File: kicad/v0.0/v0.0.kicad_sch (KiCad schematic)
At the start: 18 parts, among them M1 MNMOS, M2 MNMOS, U1 OPAMP, U2 MAX14872ETC+, U3 NE555D

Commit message: kicad stuff
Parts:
- added C?: 1uF, Capacitor_SMD:C_0805_2012Metric_Pad1.18x1.45mm_HandSolder, symbol Device:C_Small
- added J?: BUTTON, Connector_Molex:Molex_KK-254_AE-6410-02A_1x02_P2.54mm_Vertical, symbol Connector_Generic:Conn_01x02
- added R?: 10k, Resistor_SMD:R_0805_2012Metric_Pad1.20x1.40mm_HandSolder, symbol Device:R
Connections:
- net GND: now also C?.2, J?.1 (Pin_1)
- net at U2.6 (REV): now also M2.4 (B); no longer M2.1 (D)
- net at M1.1 (D), U3.3 (Q): now also M2.1 (D); no longer M2.3 (S), M2.4 (B)
- new net: J?.2 (Pin_2), R?.1
- new net BUTTON: C?.1, R?.2
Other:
- note added: "BUTTON"
- note added: "LED"
- note added: "MOTOR CONTROLLER"
- note added: "POWER/STEP-DOWN"
- note added: "PROCESSOR CONNECTORS"
- note removed: "MOTOR IC"
- note removed: "must choose R that keeps |V_COM| < 250mV"
- note removed: "use FAULT to tell microP that theres a problem? or just ground FAULT and CPU ignores if theres an error?"
- moved on the sheet: C1, C2, C3, D1, D2, D3, D4, M1, M2, R3, R4, R5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

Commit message: v0.0 is done (i think)! also added a Documents folder to store datasheets and such
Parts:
- added J?: ESP8266_left, symbol Connector:Conn_01x15_Female
- added J?: USB_B_Micro, symbol Connector:USB_B_Micro
- added J?: LED, symbol Connector:Conn_01x02_Male
- added J?: ESP8266_right, symbol Connector:Conn_01x15_Female
- added R? (x2): 10k, symbol Device:R
- added R?: R, symbol Device:R
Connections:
- net +5V: now also J?.1 (VBUS)
- net BUTTON: now also J?.2 (Pin_2)
- net FWD: now also J?.3 (Pin_3)
- net GND: now also J?.1 (Pin_1), J?.10 (Pin_10), J?.14 (Pin_14), J?.14 (Pin_14), J?.5 (GND), J?.7 (Pin_7), R?.2, R?.2, R?.2
- net REV: now also J?.4 (Pin_4)
- net V_PHOTO: now also J?.1 (Pin_1)
- new net: J?.2 (D-), R?.1
- new net: J?.3 (D+), R?.1
- new net: J?.6 (Shield), R?.1
- new net: J?.13 (Pin_13), J?.2 (Pin_2)
- new net 3V3: J?.11 (Pin_11), J?.15 (Pin_15), J?.6 (Pin_6)
- new net A0: J?.1 (Pin_1)
- new net CLK: J?.9 (Pin_9)
- new net CMD: J?.7 (Pin_7)
- new net D4: J?.5 (Pin_5)
- new net D5: J?.8 (Pin_8)
- new net D6: J?.9 (Pin_9)
- new net D7: J?.10 (Pin_10)
- new net D8: J?.11 (Pin_11)
- new net D9: J?.12 (Pin_12)
- new net EN: J?.12 (Pin_12)
- new net RST: J?.13 (Pin_13)
- new net RSV: J?.2 (Pin_2), J?.3 (Pin_3)
- new net SD0: J?.8 (Pin_8)
- new net SD1: J?.6 (Pin_6)
- new net SD2: J?.5 (Pin_5)
- new net SD3: J?.4 (Pin_4)
- new net Vin: J?.15 (Pin_15)
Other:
- note added: "POWER"
- note removed: "LED"
- note removed: "POWER/STEP-DOWN"
- moved on the sheet: C?, J?, R?

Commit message: forgot to save in kicad before sending files here... awk
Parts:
- removed J?: USB_B_Micro, symbol Connector:USB_B_Micro
- removed R? (x2): 10k, symbol Device:R
- removed R?: R, symbol Device:R
- added C5: 470u, symbol pspice:C
- added C6: 220u, symbol pspice:C
- added D5: D_Schottky, symbol Device:D_Schottky
- added J2: 9V_IN, symbol Connector:Barrel_Jack
- added L1: 68u, symbol pspice:INDUCTOR
- added U4: LM2596S-5, Package_TO_SOT_SMD:TO-263-5_TabPin3, symbol Regulator_Switching:LM2596S-5
- gave numbers to parts that had none: 6
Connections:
- net +5V: now also C6.1, L1.2, U4.4 (FB)
- net GND: now also C5.1, C6.2, D5.2 (A), J2.2, U4.3 (GND), U4.5 (~{ON}/OFF)
- new net: D5.1 (K), L1.1, U4.2 (OUT)
- new net +9V: C5.2, J2.1, U4.1 (VIN)
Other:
- note added: "POWER INPUT"
- note removed: "POWER"

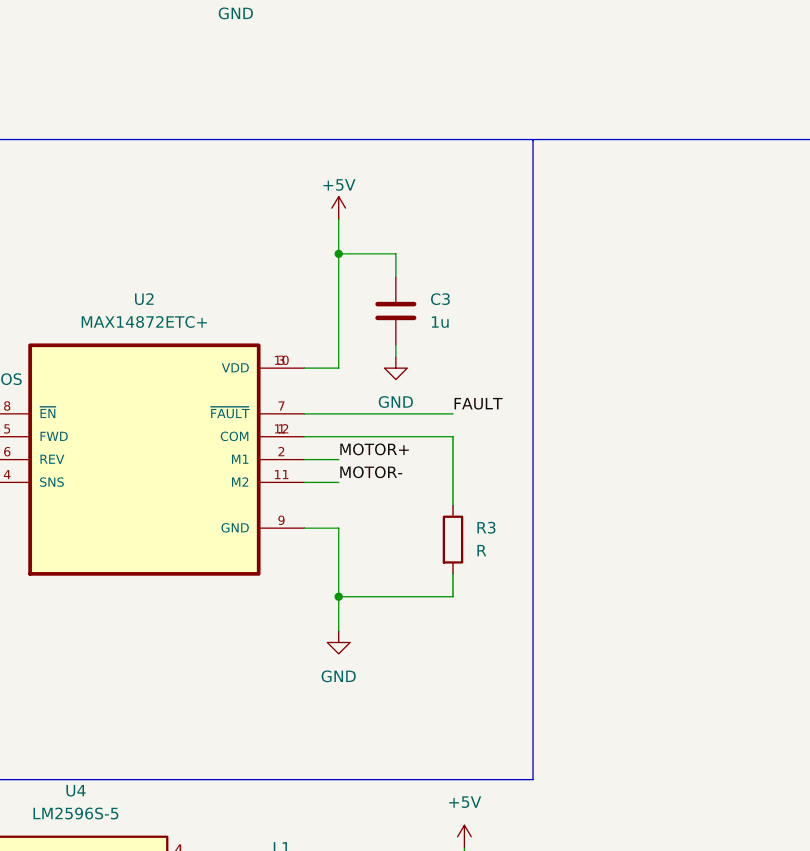
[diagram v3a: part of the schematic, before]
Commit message: updated motor to be 9V
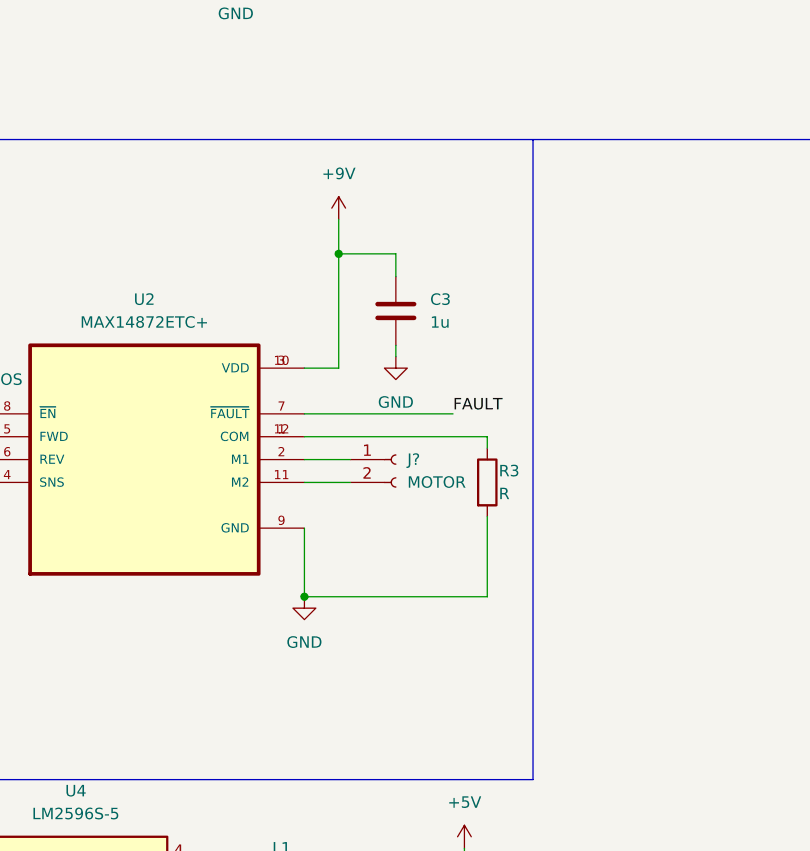
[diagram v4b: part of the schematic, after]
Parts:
- added J?: MOTOR, symbol Connector:Conn_01x02_Female
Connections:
- net +5V: no longer C3.1, U2.10 (VDD), U2.3 (VDD)
- net +9V: now also C3.1, U2.10 (VDD), U2.3 (VDD)
- net MOTOR+: no longer names the net of U2.2 (M1)
- net MOTOR+: now also J?.1 (Pin_1)
- net MOTOR-: no longer names the net of U2.11 (M2)
- net MOTOR-: now also J?.2 (Pin_2)
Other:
- moved on the sheet: R3
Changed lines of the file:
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@@
   (junction (at 39.37 181.61) (diameter 0) (color 0 0 0 0)
   )
+  (junction (at 153.67 144.78) (diameter 0) (color 0 0 0 0)
+  )
   (junction (at 100.33 193.04) (diameter 0) (color 0 0 0 0)
   )
-  (junction (at 157.48 144.78) (diameter 0) (color 0 0 0 0)
-  )
   (junction (at 45.72 114.3) (diameter 0) (color 0 0 0 0)
   )
@@
     (stroke (width 0) (type default) (color 0 0 0 0))
   )
+  (wire (pts (xy 173.99 128.27) (xy 173.99 127))
+    (stroke (width 0) (type default) (color 0 0 0 0))
+  )
   (wire (pts (xy 15.24 105.41) (xy 21.59 105.41))
     (stroke (width 0) (type default) (color 0 0 0 0))
@@
     (stroke (width 0) (type default) (color 0 0 0 0))
   )
+  (wire (pts (xy 153.67 137.16) (xy 153.67 144.78))
+    (stroke (width 0) (type default) (color 0 0 0 0))
+  )
   (wire (pts (xy 100.33 179.07) (xy 100.33 193.04))
     (stroke (width 0) (type default) (color 0 0 0 0))
@@
     (stroke (width 0) (type default) (color 0 0 0 0))
   )
+  (wire (pts (xy 153.67 132.08) (xy 158.75 132.08))
+    (stroke (width 0) (type default) (color 0 0 0 0))
+  )
   (wire (pts (xy 73.66 43.18) (xy 77.47 43.18))
     (stroke (width 0) (type default) (color 0 0 0 0))
@@
     (stroke (width 0) (type default) (color 0 0 0 0))
   )
+  (wire (pts (xy 153.67 144.78) (xy 173.99 144.78))
+    (stroke (width 0) (type default) (color 0 0 0 0))
+  )
   (wire (pts (xy 110.49 187.96) (xy 110.49 193.04))
     (stroke (width 0) (type default) (color 0 0 0 0))
@@
     (stroke (width 0) (type default) (color 0 0 0 0))
   )
-  (wire (pts (xy 157.48 144.78) (xy 157.48 148.59))
-    (stroke (width 0) (type default) (color 0 0 0 0))
-  )
   (wire (pts (xy 29.21 105.41) (xy 33.02 105.41))
     (stroke (width 0) (type default) (color 0 0 0 0))
@@
     (stroke (width 0) (type default) (color 0 0 0 0))
   )
-  (wire (pts (xy 153.67 132.08) (xy 157.48 132.08))
-    (stroke (width 0) (type default) (color 0 0 0 0))
-  )
   (wire (pts (xy 52.07 121.92) (xy 52.07 114.3))
     (stroke (width 0) (type default) (color 0 0 0 0))
@@
     (stroke (width 0) (type default) (color 0 0 0 0))
   )
-  (wire (pts (xy 157.48 137.16) (xy 153.67 137.16))
-    (stroke (width 0) (type default) (color 0 0 0 0))
-  )
   (wire (pts (xy 165.1 179.07) (xy 165.1 173.99))
     (stroke (width 0) (type default) (color 0 0 0 0))
@@
     (stroke (width 0) (type default) (color 0 0 0 0))
   )
-  (wire (pts (xy 170.18 127) (xy 170.18 134.62))
-    (stroke (width 0) (type default) (color 0 0 0 0))
-  )
-  (wire (pts (xy 170.18 142.24) (xy 170.18 144.78))
-    (stroke (width 0) (type default) (color 0 0 0 0))
-  )
   (wire (pts (xy 142.24 189.23) (xy 142.24 193.04))
     (stroke (width 0) (type default) (color 0 0 0 0))
@@
     (stroke (width 0) (type default) (color 0 0 0 0))
   )
-  (wire (pts (xy 153.67 129.54) (xy 157.48 129.54))
+  (wire (pts (xy 153.67 129.54) (xy 158.75 129.54))
     (stroke (width 0) (type default) (color 0 0 0 0))
   )
@@
     (stroke (width 0) (type default) (color 0 0 0 0))
   )
-  (wire (pts (xy 153.67 127) (xy 170.18 127))
+  (wire (pts (xy 153.67 127) (xy 173.99 127))
     (stroke (width 0) (type default) (color 0 0 0 0))
   )
@@
     (stroke (width 0) (type default) (color 0 0 0 0))
   )
-  (wire (pts (xy 157.48 144.78) (xy 170.18 144.78))
-    (stroke (width 0) (type default) (color 0 0 0 0))
-  )
   (wire (pts (xy 49.53 139.7) (xy 52.07 139.7))
     (stroke (width 0) (type default) (color 0 0 0 0))
@@
     (stroke (width 0) (type default) (color 0 0 0 0))
   )
-  (wire (pts (xy 157.48 137.16) (xy 157.48 144.78))
+  (wire (pts (xy 173.99 135.89) (xy 173.99 144.78))
     (stroke (width 0) (type default) (color 0 0 0 0))
   )
@@
     (effects (font (size 1.27 1.27)) (justify left bottom))
   )
-  (label "MOTOR-" (at 157.48 132.08 0)
-    (effects (font (size 1.27 1.27)) (justify left bottom))
-  )
   (label "3V3" (at 177.8 66.04 0)
     (effects (font (size 1.27 1.27)) (justify left bottom))
@@
   )
   (label "BUTTON" (at 44.45 181.61 0)
-    (effects (font (size 1.27 1.27)) (justify left bottom))
-  )
-  (label "MOTOR+" (at 157.48 129.54 0)
     (effects (font (size 1.27 1.27)) (justify left bottom))
   )
@@
     )
     (property "Datasheet" "" (id 3) (at 163.83 118.11 0)
+      (effects (font (size 1.27 1.27)) hide)
+    )
+    (pin "1")
+  )
+  (symbol (lib_id "power:+9V") (at 157.48 102.87 0) (unit 1)
+    (in_bom yes) (on_board yes) (fields_autoplaced)
+    (property "Reference" "#PWR?" (id 0) (at 157.48 106.68 0)
+      (effects (font (size 1.27 1.27)) hide)
+    )
+    (property "Value" "+9V" (id 1) (at 157.48 97.79 0))
+    (property "Footprint" "" (id 2) (at 157.48 102.87 0)
+      (effects (font (size 1.27 1.27)) hide)
+    )
+    (property "Datasheet" "" (id 3) (at 157.48 102.87 0)
       (effects (font (size 1.27 1.27)) hide)
     )
@@
     (pin "2")
   )
+  (symbol (lib_id "Connector:Conn_01x02_Female") (at 163.83 129.54 0) (unit 1)
+    (in_bom yes) (on_board yes) (fields_autoplaced)
+    (property "Reference" "J?" (id 0) (at 165.1 129.5399 0)
+      (effects (font (size 1.27 1.27)) (justify left))
+    )
+    (property "Value" "MOTOR" (id 1) (at 165.1 132.0799 0)
+      (effects (font (size 1.27 1.27)) (justify left))
+    )
+    (property "Footprint" "" (id 2) (at 163.83 129.54 0)
+      (effects (font (size 1.27 1.27)) hide)
+    )
+    (property "Datasheet" "~" (id 3) (at 163.83 129.54 0)
+      (effects (font (size 1.27 1.27)) hide)
+    )
+    (pin "1")
+    (pin "2")
+  )
   (symbol (lib_id "Connector_Generic:Conn_01x02") (at 21.59 184.15 180) (unit 1)
     (in_bom yes) (on_board yes) (fields_autoplaced)
@@
     (pin "1")
     (pin "2")
-  )
-  (symbol (lib_id "power:+5V") (at 157.48 102.87 0) (unit 1)
-    (in_bom yes) (on_board yes)
-    (property "Reference" "#PWR06" (id 0) (at 157.48 106.68 0)
-      (effects (font (size 1.27 1.27)) hide)
-    )
-    (property "Value" "+5V" (id 1) (at 157.48 99.06 0))
-    (property "Footprint" "" (id 2) (at 157.48 102.87 0)
-      (effects (font (size 1.27 1.27)) hide)
-    )
-    (property "Datasheet" "" (id 3) (at 157.48 102.87 0)
-      (effects (font (size 1.27 1.27)) hide)
-    )
-    (pin "1")
   )
   (symbol (lib_id "Device:D") (at 52.07 125.73 270) (unit 1)
@@
     (pin "2")
   )
-  (symbol (lib_id "power:GND") (at 157.48 148.59 0) (unit 1)
-    (in_bom yes) (on_board yes) (fields_autoplaced)
-    (property "Reference" "#PWR07" (id 0) (at 157.48 154.94 0)
-      (effects (font (size 1.27 1.27)) hide)
-    )
-    (property "Value" "GND" (id 1) (at 157.48 153.67 0))
-    (property "Footprint" "" (id 2) (at 157.48 148.59 0)
-      (effects (font (size 1.27 1.27)) hide)
-    )
-    (property "Datasheet" "" (id 3) (at 157.48 148.59 0)
-      (effects (font (size 1.27 1.27)) hide)
-    )
-    (pin "1")
-  )
-  (symbol (lib_id "Device:R") (at 170.18 138.43 0) (unit 1)
+  (symbol (lib_id "power:GND") (at 153.67 144.78 0) (unit 1)
+    (in_bom yes) (on_board yes) (fields_autoplaced)
+    (property "Reference" "#PWR07" (id 0) (at 153.67 151.13 0)
+      (effects (font (size 1.27 1.27)) hide)
+    )
+    (property "Value" "GND" (id 1) (at 153.67 149.86 0))
+    (property "Footprint" "" (id 2) (at 153.67 144.78 0)
+      (effects (font (size 1.27 1.27)) hide)
+    )
+    (property "Datasheet" "" (id 3) (at 153.67 144.78 0)
+      (effects (font (size 1.27 1.27)) hide)
+    )
+    (pin "1")
+  )
+  (symbol (lib_id "Device:R") (at 173.99 132.08 0) (unit 1)
     (in_bom yes) (on_board yes)
-    (property "Reference" "R3" (id 0) (at 172.72 137.1599 0)
-      (effects (font (size 1.27 1.27)) (justify left))
-    )
-    (property "Value" "R" (id 1) (at 172.72 139.6999 0)
-      (effects (font (size 1.27 1.27)) (justify left))
-    )
-    (property "Footprint" "" (id 2) (at 168.402 138.43 90)
-      (effects (font (size 1.27 1.27)) hide)
-    )
-    (property "Datasheet" "~" (id 3) (at 170.18 138.43 0)
+    (property "Reference" "R3" (id 0) (at 175.26 130.81 0)
+      (effects (font (size 1.27 1.27)) (justify left))
+    )
+    (property "Value" "R" (id 1) (at 175.26 133.35 0)
+      (effects (font (size 1.27 1.27)) (justify left))
+    )
+    (property "Footprint" "" (id 2) (at 172.212 132.08 90)
+      (effects (font (size 1.27 1.27)) hide)
+    )
+    (property "Datasheet" "~" (id 3) (at 173.99 132.08 0)
       (effects (font (size 1.27 1.27)) hide)
     )
@@
       (reference "#PWR05") (unit 1) (value "GND") (footprint "")
     )
-    (path "/75e492af-88e2-417e-b9ca-2ba118786ea4"
-      (reference "#PWR06") (unit 1) (value "+5V") (footprint "")
-    )
     (path "/be4aa998-2cb7-4ac8-9eb1-539794bb05e9"
       (reference "#PWR07") (unit 1) (value "GND") (footprint "")
@@
       (reference "#PWR018") (unit 1) (value "+5V") (footprint "")
     )
+    (path "/137c0f8b-4469-49b8-b0dc-b79970d0302a"
+      (reference "#PWR?") (unit 1) (value "+9V") (footprint "")
+    )
     (path "/23eaba3b-0341-4969-90aa-4d5bb7d49eae"
       (reference "C1") (unit 1) (value "1u") (footprint "")
@@
       (reference "J5") (unit 1) (value "LED") (footprint "")
     )
+    (path "/71cad40e-7543-47a6-a95c-100b1765fa37"
+      (reference "J?") (unit 1) (value "MOTOR") (footprint "")
+    )
     (path "/73d0ccac-0d54-431e-a77a-e37ff7550bbd"

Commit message: all footprints assigned except for potentiometer
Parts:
- removed C1: 1u, symbol Device:C_Polarized
- removed C4: 1uF, Capacitor_SMD:C_0805_2012Metric_Pad1.18x1.45mm_HandSolder, symbol Device:C_Small
- removed M1, M2: MNMOS, symbol pspice:MNMOS
- removed U1: OPAMP, symbol pspice:OPAMP
- added C1, C4: 1u, Capacitor_SMD:C_0201_0603Metric_Pad0.64x0.40mm_HandSolder, symbol pspice:C
- added H1, H2, H3, H4: MountingHole, MountingHole:MountingHole_3.2mm_M3, symbol Mechanical:MountingHole
- added Q1, Q2: IRF520, TO220BV, symbol IRF520:IRF520
- added R7: 1k, Resistor_SMD:R_0603_1608Metric_Pad0.98x0.95mm_HandSolder, symbol Device:R
- C2: footprint (none) -> Capacitor_SMD:C_01005_0402Metric_Pad0.57x0.30mm_HandSolder
- C3: footprint (none) -> Capacitor_SMD:C_0201_0603Metric_Pad0.64x0.40mm_HandSolder
- C5: footprint (none) -> Capacitor_THT:CP_Radial_D10.0mm_P5.00mm
- C6: footprint (none) -> Capacitor_SMD:C_1206_3216Metric_Pad1.33x1.80mm_HandSolder
- D1, D2, D3, D4: footprint (none) -> Diode_SMD:D_SMA_Handsoldering
- D5: footprint (none) -> Diode_SMD:D_SOD-323_HandSoldering
- J2: footprint (none) -> Connector_BarrelJack:BarrelJack_CUI_PJ-063AH_Horizontal
- J3, J4: footprint (none) -> Connector_PinSocket_2.54mm:PinSocket_1x15_P2.54mm_Vertical
- J5: footprint (none) -> Connector_PinSocket_2.54mm:PinSocket_1x02_P2.54mm_Horizontal
- J6: renamed from J?; footprint (none) -> Connector_PinSocket_2.54mm:PinSocket_1x02_P2.54mm_Horizontal
- L1: footprint (none) -> Inductor_SMD:L_Bourns_SDR1806
- R1, R4, R5: footprint (none) -> Resistor_SMD:R_0603_1608Metric_Pad0.98x0.95mm_HandSolder
- R2: footprint (none) -> OptoDevice:R_LDR_5.1x4.3mm_P3.4mm_Vertical
- R3: value R -> 1k; footprint (none) -> Resistor_SMD:R_0603_1608Metric_Pad0.98x0.95mm_HandSolder
- R6: footprint Resistor_SMD:R_0805_2012Metric_Pad1.20x1.40mm_HandSolder -> Resistor_SMD:R_0201_0603Metric_Pad0.64x0.40mm_HandSolder
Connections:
- net BUTTON: now also C4.1
- net FWD: now also Q2.G
- net GND: now also C4.2
- net REV: now also Q1.G
- net V_PHOTO: now also R7.2
- net at RV1.2, U3.2 (TR), U3.6 (THR): now also C1.1
- net at U2.5 (FWD): now also Q2.S
- net at U2.6 (REV): now also Q1.S
- net at U3.3 (Q): now also Q1.D, Q2.D
- net at R1.1, R2.2: now also R7.1
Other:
- note added: "PHOTORESISTOR READ"
- note removed: "PHOTODIODE READ"
- note removed: "The opamp restricts current from flowing into the microprocessor while allowing us to still read the voltage drop across the 1k resistor (not sure if necessary, but adds extra level of protection to the microP)"

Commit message: finally found some pot
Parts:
- RV1: footprint (none) -> Potentiometer_THT:Potentiometer_Bourns_3296W_Vertical
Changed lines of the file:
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@@
     (property "Reference" "RV1" (id 0) (at 45.72 133.35 90))
     (property "Value" "100k" (id 1) (at 45.72 135.89 90))
-    (property "Footprint" "" (id 2) (at 45.72 139.7 0)
+    (property "Footprint" "Potentiometer_THT:Potentiometer_Bourns_3296W_Vertical" (id 2) (at 45.72 139.7 0)
       (effects (font (size 1.27 1.27)) hide)
     )
@@
     )
     (path "/0453f108-7dce-491b-878b-92849be18fad"
-      (reference "RV1") (unit 1) (value "100k") (footprint "")
+      (reference "RV1") (unit 1) (value "100k") (footprint "Potentiometer_THT:Potentiometer_Bourns_3296W_Vertical")
     )
     (path "/20935cf2-ab8a-474f-bf12-ce3a5ccf7d28"
